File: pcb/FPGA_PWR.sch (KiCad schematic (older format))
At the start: 33 parts, among them J7 JSHORTNORMAL, U4 iCE40-HX8K-CT256

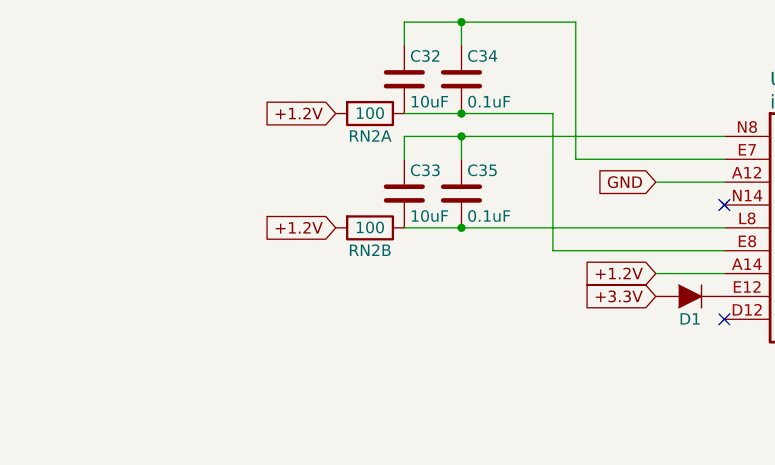
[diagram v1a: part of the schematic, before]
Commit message: Most components placed. FPGA + SDRAM + routing placed off-board.
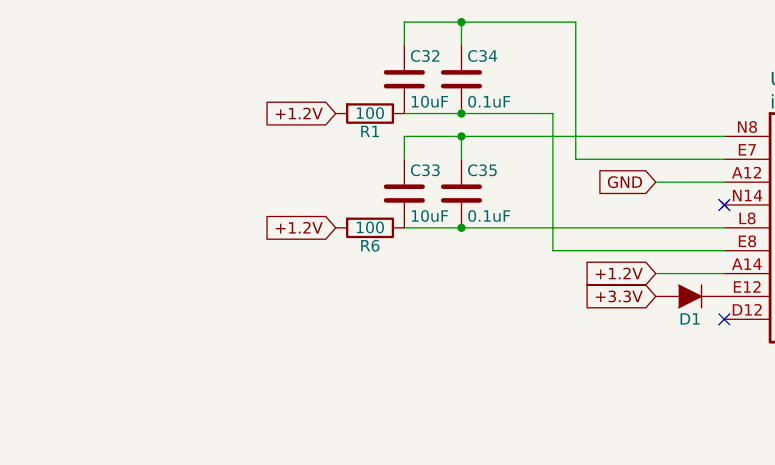
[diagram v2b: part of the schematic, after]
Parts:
- removed RN2: 100, XESS:CTS_742C043, symbol RN2
- added R1, R6: 100, Resistors_SMD:R_0603, symbol R
- C16, C17, C18, C19, C20, C21, C22, C23, C24, C25, C26, C27, C28, C29, C30, C31, C34, C35, C38, C39, C40, C41, C42, C43, C44, C45, C46: footprint Capacitors_SMD:C_0603_HandSoldering -> Capacitors_SMD:C_0603
- C32, C33: footprint Capacitors_SMD:C_0603_HandSoldering -> Capacitors_SMD:C_0805
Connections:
- net +1.2V: now also R1.2, R6.2
- net at C32.2, C34.2, U4.E8 (VCCPLL1): now also R1.1
- net at C33.2, C35.2, U4.L8 (VCCPLL0): now also R6.1

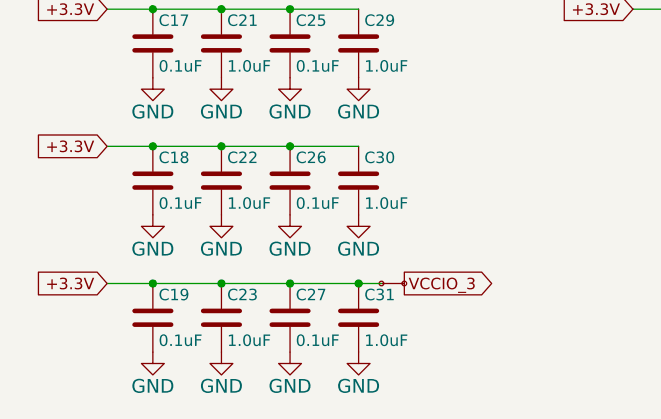
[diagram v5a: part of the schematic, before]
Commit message: Split power planes built. * Capacitors approximately placed.
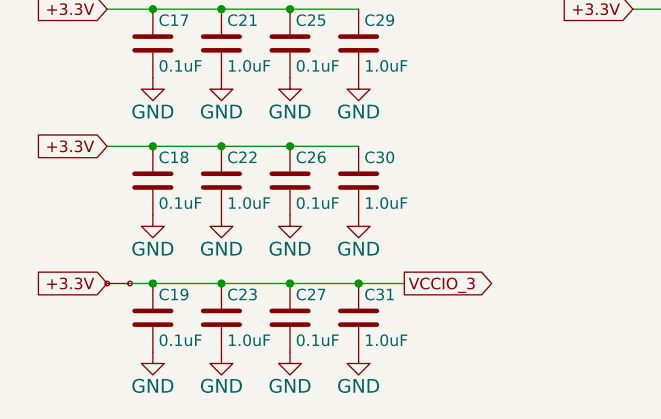
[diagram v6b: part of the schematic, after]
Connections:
- net +3.3V: no longer C19.1, C23.1, C27.1, C31.1
- net VCCIO_3: now also C19.1, C23.1, C27.1, C31.1
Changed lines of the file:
@@
 L JSHORTNORMAL J7
 U 1 1 55F0E8FA
-P 5200 5500
-F 0 "J7" H 5100 5575 50  0001 L BNN
-F 1 "JSHORTNORMAL" H 5100 5400 50  0001 L BNN
-F 2 "XESS:xess-JSHORT" H 5200 5650 50  0001 C CNN
-F 3 "" H 5200 5500 60  0000 C CNN
-	1    5200 5500
+P 4000 5500
+F 0 "J7" H 3900 5575 50  0001 L BNN
+F 1 "JSHORTNORMAL" H 3900 5400 50  0001 L BNN
+F 2 "XESS:xess-JSHORT" H 4000 5650 50  0001 C CNN
+F 3 "" H 4000 5500 60  0000 C CNN
+	1    4000 5500
 	1    0    0    -1
 $EndComp
-Wire Wire Line
-	4000 5500 5200 5500
-Connection ~ 4200 5500
-Connection ~ 4500 5500
-Connection ~ 4800 5500
-Connection ~ 5100 5500
 Text GLabel 5300 5500 2    50   Output ~ 0
 VCCIO_3
@@
 1E 25 49 2A DA F6 C4 5C B7 0C C3 B9 A4 0A 98 09 FC 0D B0 92 CD 57 CD 1F 06 4E 04 26 A7 75 27 49
 52 39 26 13 73 DE C3 6C BE 70 B5 12 F8 16 86 73 8D C3 FF 03 63 F8 EE 2E BE 9A 04 B1 00 00 00 00
-49 45 4E 44 AE 42 60 82 46
+49 45 4E 44 AE 42 60 82 E6
 EndData
 $EndBitmap
@@
 	0    1    1    0
 $EndComp
+Wire Wire Line
+	4100 5500 5300 5500
+Connection ~ 5100 5500
+Connection ~ 4800 5500
+Connection ~ 4500 5500
+Connection ~ 4200 5500
 $EndSCHEMATC

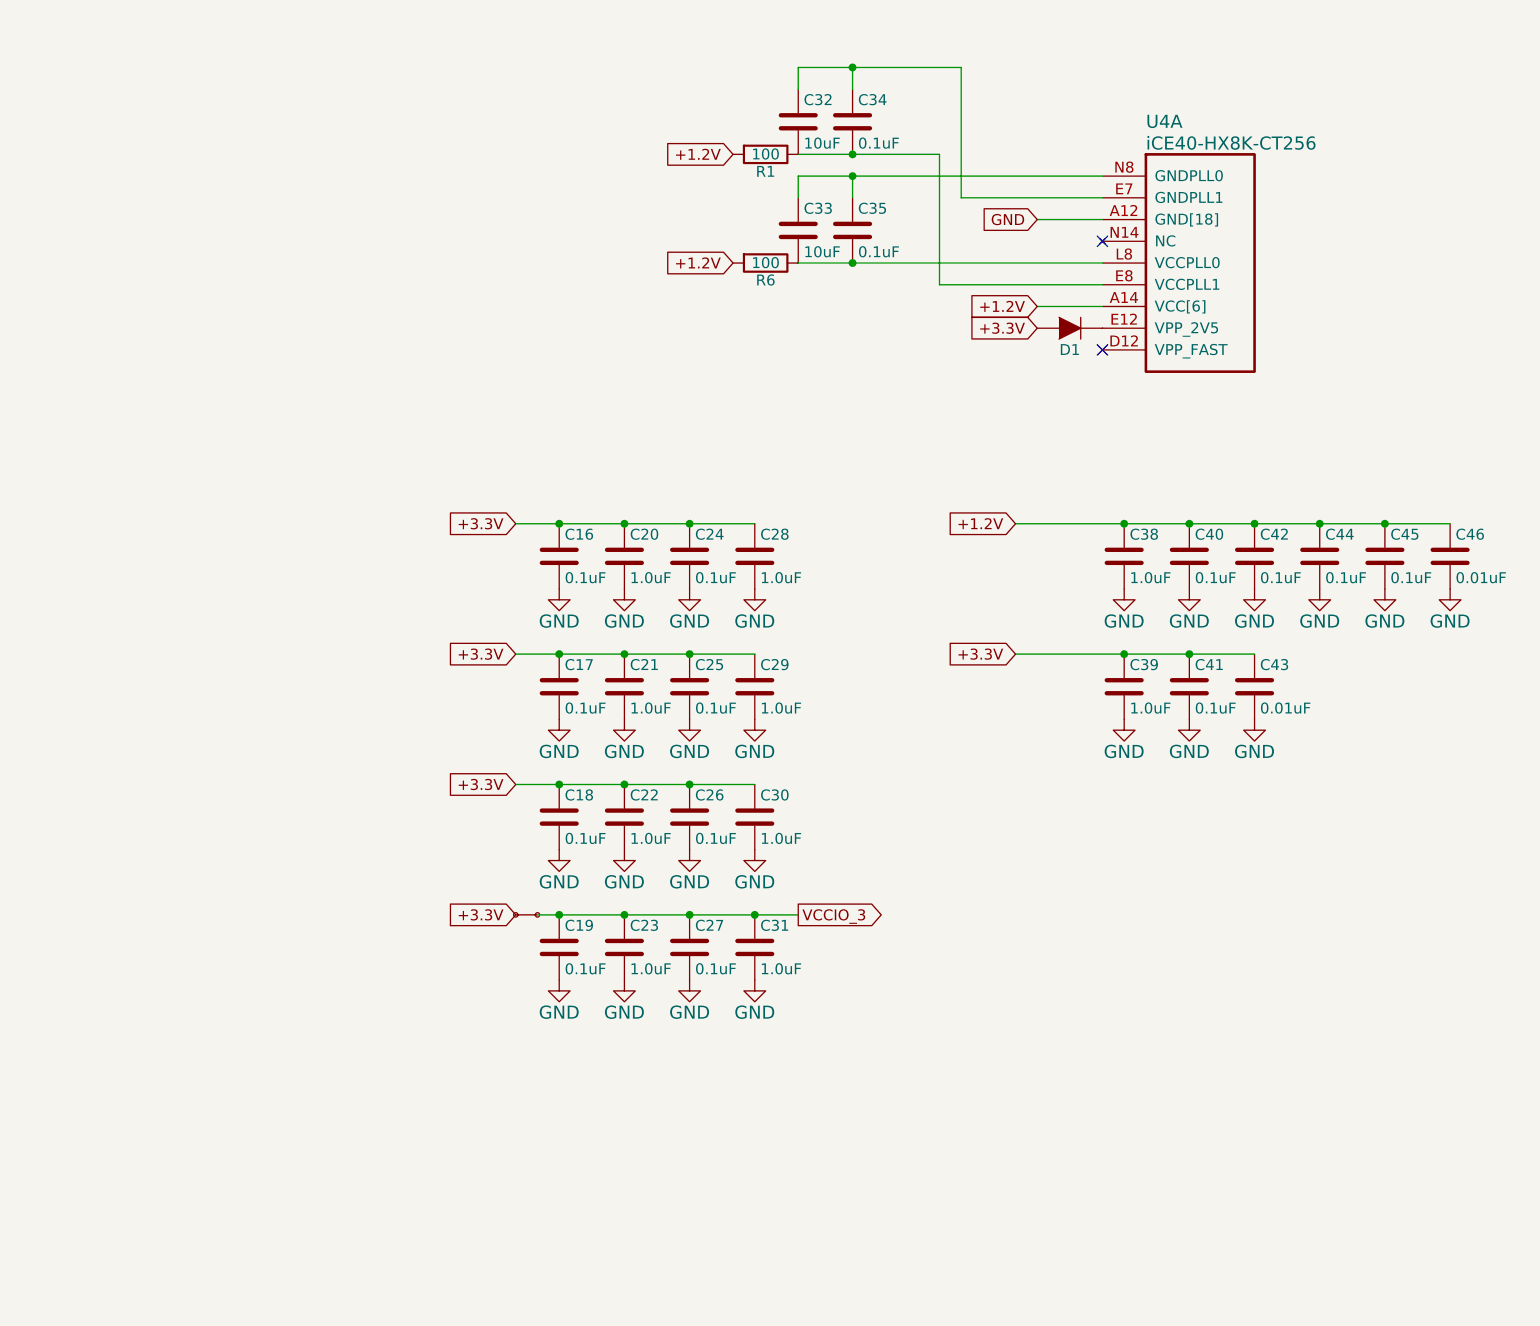
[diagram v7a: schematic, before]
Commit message: All layout done except for placing test points and arranging silkscreen.
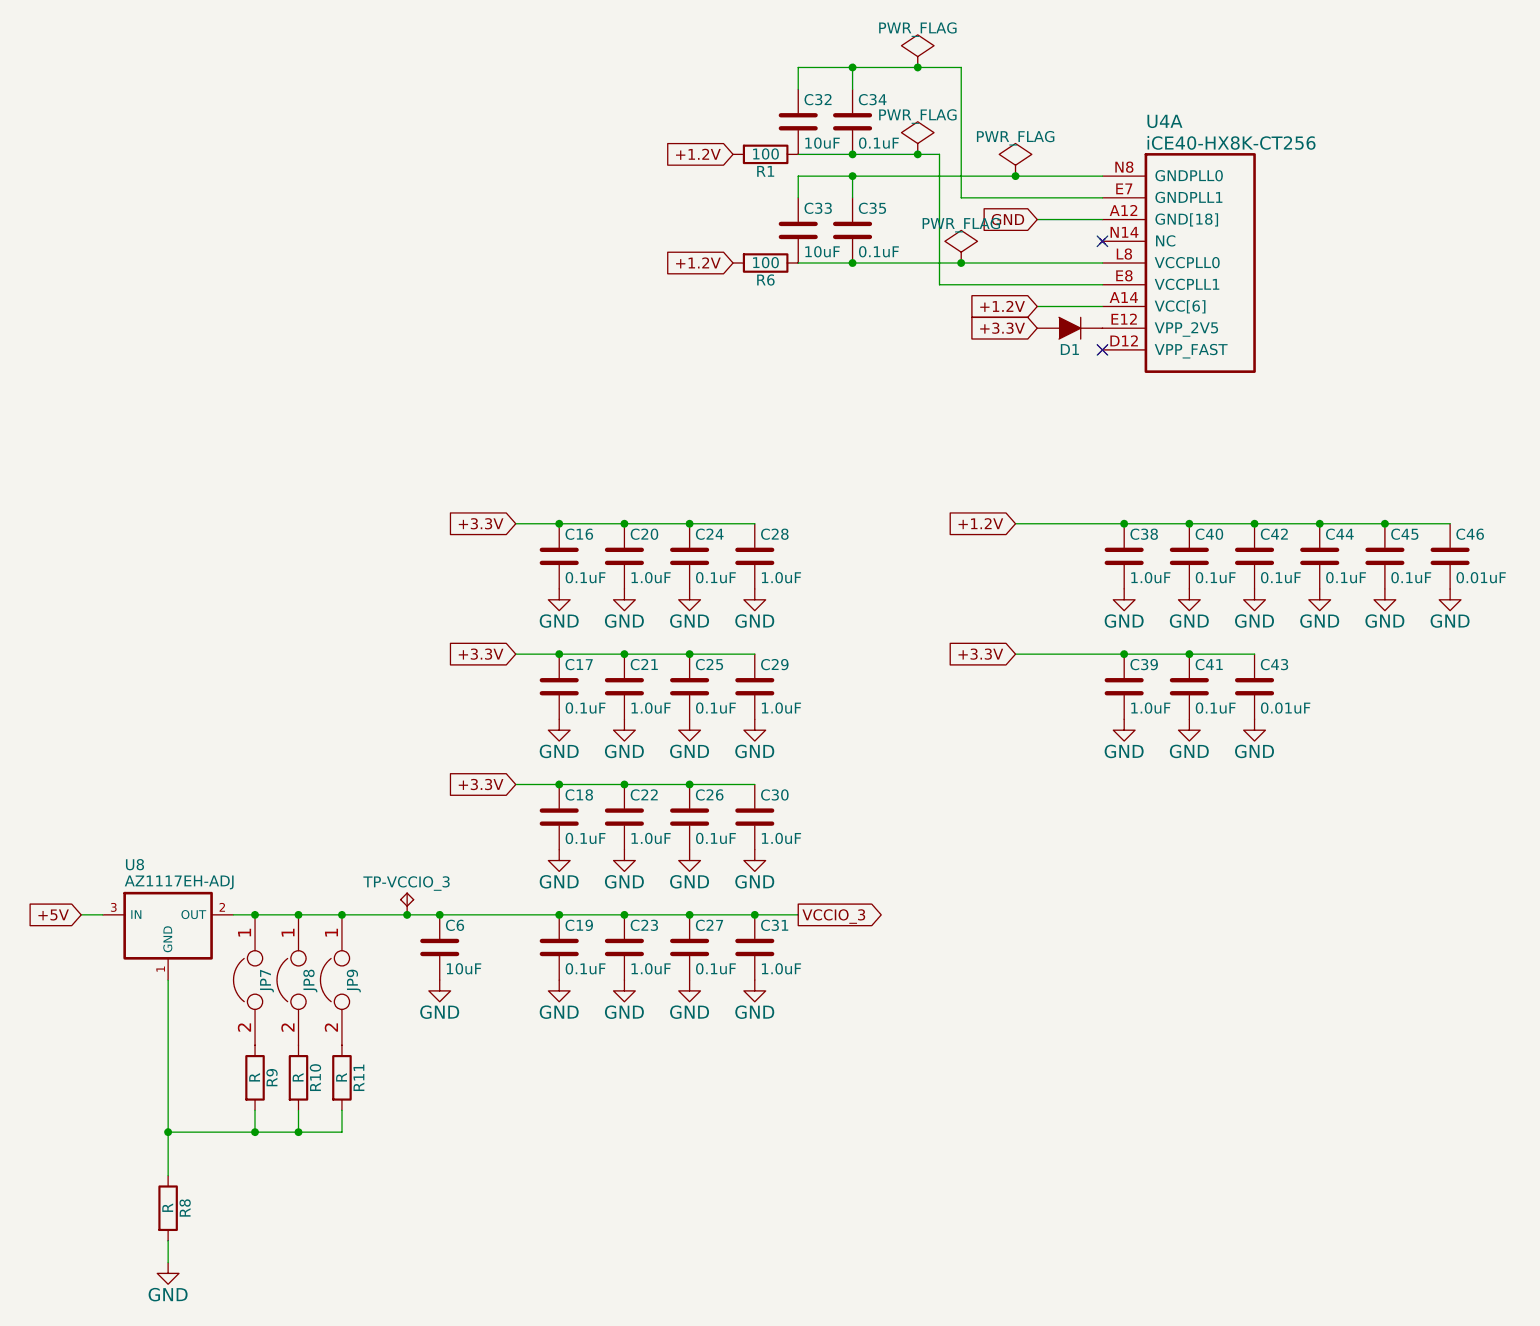
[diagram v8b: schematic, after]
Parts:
- removed J7: JSHORTNORMAL, XESS:xess-JSHORT, symbol JSHORTNORMAL
- added C6: 10uF, Capacitors_SMD:C_0805, symbol C
- added JP7, JP8, JP9: JUMPER, open-project:S_JUMPER_2, symbol JUMPER
- added R10, R11, R8, R9: R, Resistors_SMD:R_0603, symbol R
- added TP-VCCIO_3: TPTP-COMPACT, Measurement_Points:Measurement_Point_Round-TH_Small, symbol TPTP-COMPACT
- added U8: AZ1117EH-ADJ, XESS:SOT-223, symbol NCV1117
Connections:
- net GND: now also C6.2, R8.2
- net VCCIO_3: now also C6.1, JP7.1, JP8.1, JP9.1, TP-VCCIO_3.1 (TP), U8.2 (OUT), U8.4 (HS)
- new net: R10.2, R11.2, R8.1, R9.2, U8.1 (GND)
- new net: JP7.2, R9.1
- new net: JP8.2, R10.1
- new net: JP9.2, R11.1
- new net +5V: U8.3 (IN)
